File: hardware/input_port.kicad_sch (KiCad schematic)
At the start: 5 parts, among them J101 SS-74500-022

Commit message: Save
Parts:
- renumbered J101 to J301

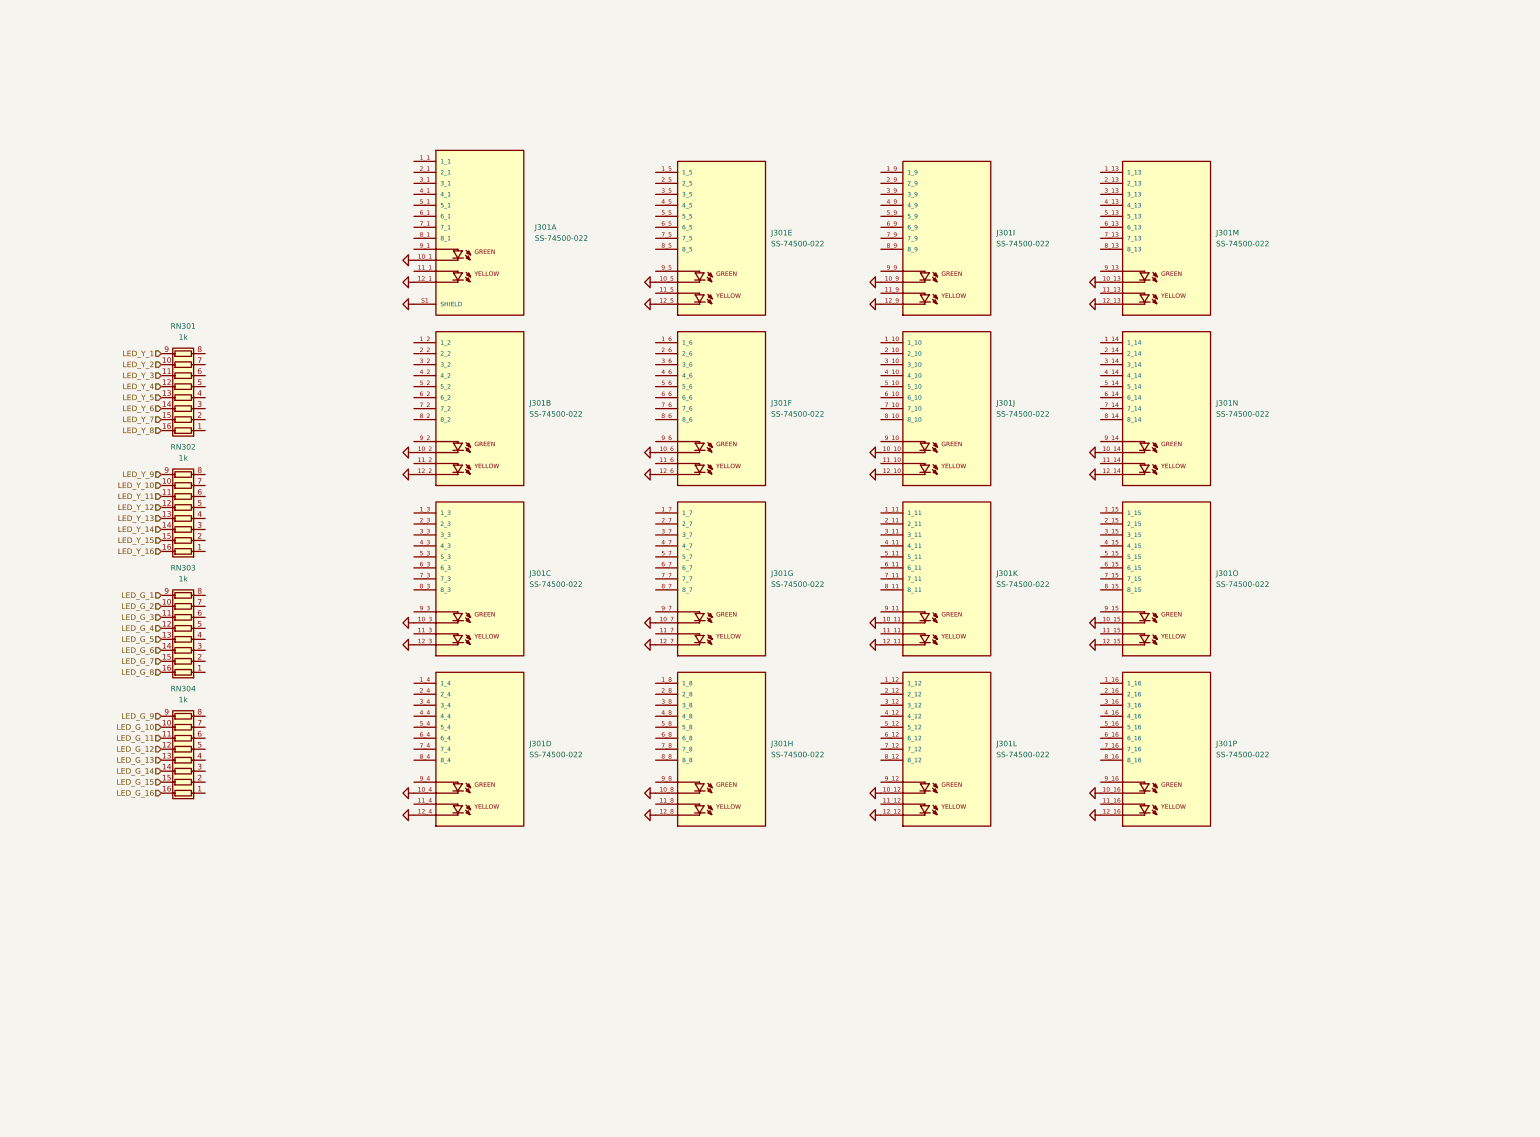
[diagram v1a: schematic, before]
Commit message: Moved to PCIe connectors, added USB 3.0 Type B connector
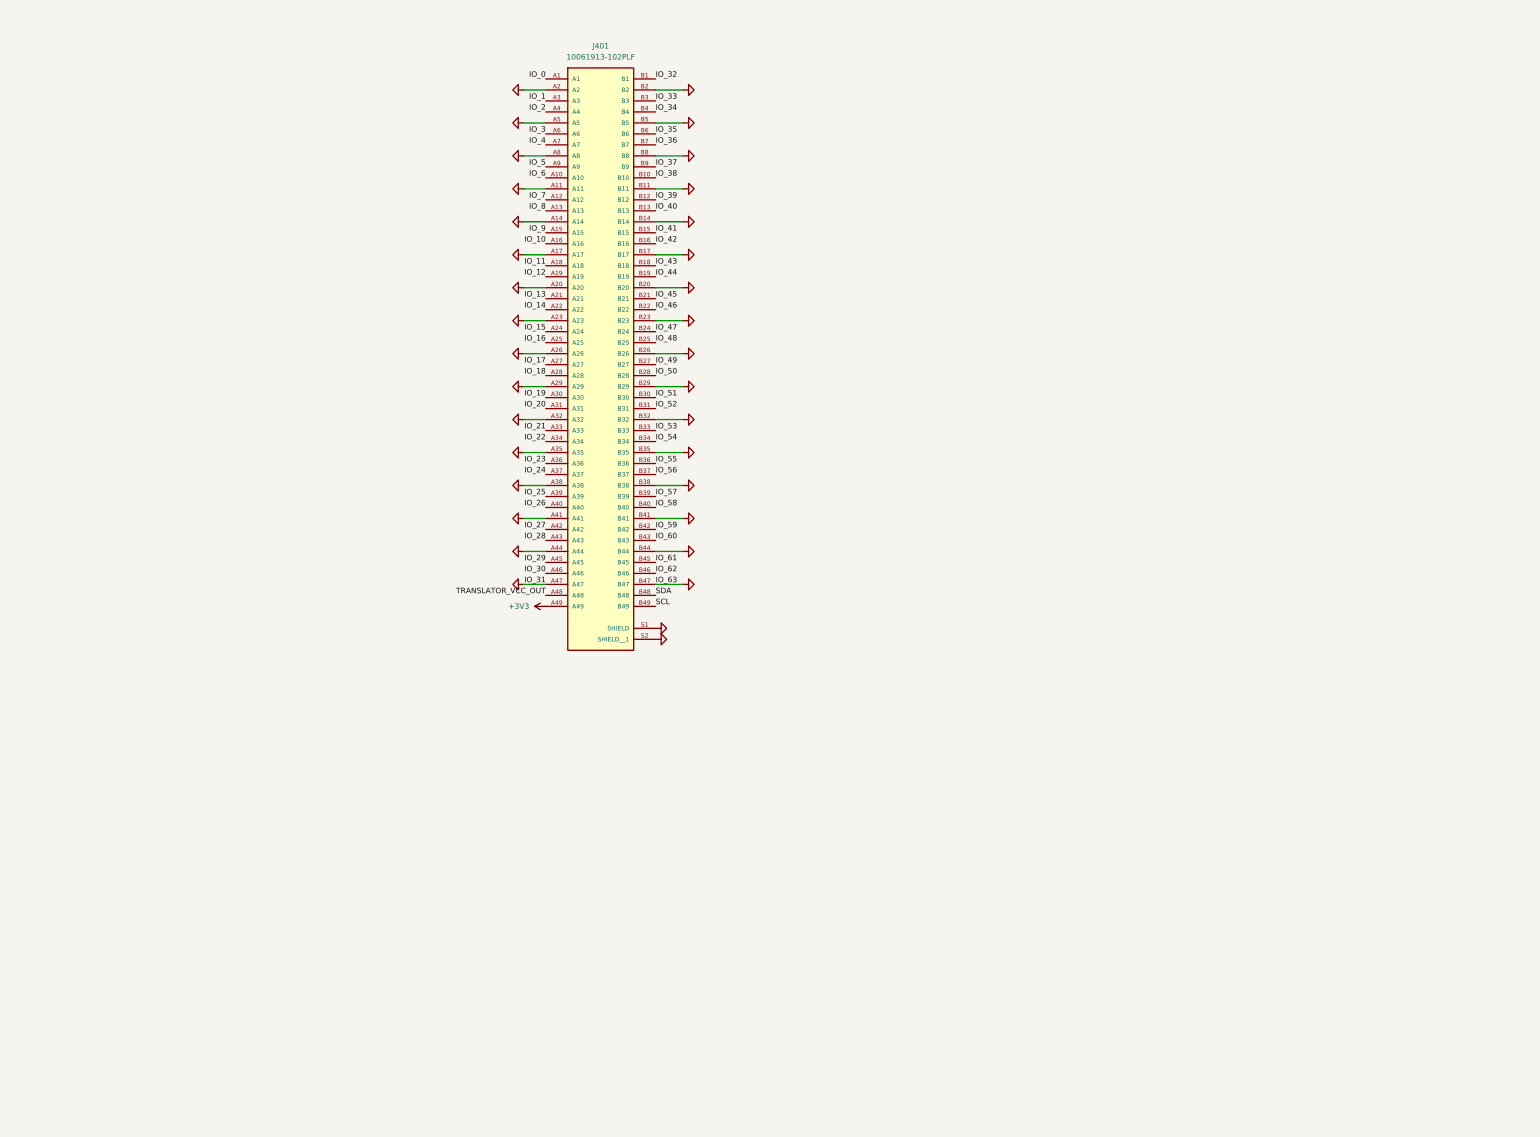
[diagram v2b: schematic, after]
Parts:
- removed J301: SS-74500-022, BEL_SS-74500-022, symbol connectors:SS-74500-022
- removed RN301, RN302, RN303, RN304: 1k, Resistor_SMD:R_Array_Convex_8x0602, symbol Device:R_Pack08
- added J401: 10061913-102PLF, connectors:AMPHENOL_10061913-102PLF, symbol connectors:10061913-102PLF
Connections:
- net GND: now also J401.A11, J401.A14, J401.A17, J401.A2, J401.A20, J401.A23, J401.A26, J401.A29, J401.A32, J401.A35, J401.A38, J401.A41, J401.A44, J401.A47, J401.A5, J401.A8, J401.B11, J401.B14, J401.B17, J401.B2, J401.B20, J401.B23, J401.B26, J401.B29, J401.B32, J401.B35, J401.B38, J401.B41, J401.B44, J401.B47, J401.B5, J401.B8, J401.S1 (SHIELD), J401.S2 (SHIELD__1)
- new net +3V3: J401.A49
- new net IO_0: J401.A1
- new net IO_1: J401.A3
- new net IO_10: J401.A16
- new net IO_11: J401.A18
- new net IO_12: J401.A19
- new net IO_13: J401.A21
- new net IO_14: J401.A22
- new net IO_15: J401.A24
- new net IO_16: J401.A25
- new net IO_17: J401.A27
- new net IO_18: J401.A28
- new net IO_19: J401.A30
- new net IO_2: J401.A4
- new net IO_20: J401.A31
- new net IO_21: J401.A33
- new net IO_22: J401.A34
- new net IO_23: J401.A36
- new net IO_24: J401.A37
- new net IO_25: J401.A39
- new net IO_26: J401.A40
- new net IO_27: J401.A42
- new net IO_28: J401.A43
- new net IO_29: J401.A45
- new net IO_3: J401.A6
- new net IO_30: J401.A46
- new net IO_32: J401.B1
- new net IO_33: J401.B3
- new net IO_34: J401.B4
- new net IO_35: J401.B6
- new net IO_36: J401.B7
- new net IO_37: J401.B9
- new net IO_38: J401.B10
- new net IO_39: J401.B12
- new net IO_4: J401.A7
- new net IO_40: J401.B13
- new net IO_41: J401.B15
- new net IO_42: J401.B16
- new net IO_43: J401.B18
- new net IO_44: J401.B19
- new net IO_45: J401.B21
- new net IO_46: J401.B22
- new net IO_47: J401.B24
- new net IO_48: J401.B25
- new net IO_49: J401.B27
- new net IO_5: J401.A9
- new net IO_50: J401.B28
- new net IO_51: J401.B30
- new net IO_52: J401.B31
- new net IO_53: J401.B33
- new net IO_54: J401.B34
- new net IO_55: J401.B36
- new net IO_56: J401.B37
- new net IO_57: J401.B39
- new net IO_58: J401.B40
- new net IO_59: J401.B42
- new net IO_6: J401.A10
- new net IO_60: J401.B43
- new net IO_61: J401.B45
- new net IO_62: J401.B46
- new net IO_7: J401.A12
- new net IO_8: J401.A13
- new net IO_9: J401.A15
- new net SCL: J401.B49
- new net SDA: J401.B48
- new net TRANSLATOR_VCC_OUT: J401.A48

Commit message: Save
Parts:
- added C301, C302, C303, C304, C305, C306, C307, C308, C309, C310, C311, C312, C313, C314, C315, C316: 0.1u, passive:C_0201, symbol Device:C_Small
- added U301, U303, U305, U307, U309, U310, U311, U312: TXB0108DQSR, Package_SON:USON-20_2x4mm_P0.4mm, symbol Logic_LevelTranslator:TXB0108DQSR
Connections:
- net TRANSLATOR_VCC_OUT is gone; now on net GND: J401.A48
- net +3V3: now also J401.B48, C301.1, C302.1, C303.1, C304.1, C305.1, C306.1, C307.1, C308.1, U301.5 (VCCA), U303.5 (VCCA), U305.5 (VCCA), U307.5 (VCCA), U309.5 (VCCA), U310.5 (VCCA), U311.5 (VCCA), U312.5 (VCCA); no longer J401.A49
- net GND: now also C301.2, C302.2, C303.2, C304.2, C305.2, C306.2, C307.2, C308.2, C309.2, C310.2, C311.2, C312.2, C313.2, C314.2, C315.2, C316.2, U301.15 (GND), U303.15 (GND), U305.15 (GND), U307.15 (GND), U309.15 (GND), U310.15 (GND), U311.15 (GND), U312.15 (GND); no longer J401.A47, J401.B47
- net IO_0: now also U301.10 (A8); no longer J401.A1
- net IO_1: now also U301.9 (A7); no longer J401.A3
- net IO_10: now also U303.8 (A6); no longer J401.A16
- net IO_11: now also U303.7 (A5); no longer J401.A18
- net IO_12: now also U303.4 (A4); no longer J401.A19
- net IO_13: now also U303.3 (A3); no longer J401.A21
- net IO_14: now also U303.2 (A2); no longer J401.A22
- net IO_15: now also U303.1 (A1); no longer J401.A24
- net IO_16: now also U305.10 (A8); no longer J401.A25
- net IO_17: now also U305.9 (A7); no longer J401.A27
- net IO_18: now also U305.8 (A6); no longer J401.A28
- net IO_19: now also U305.7 (A5); no longer J401.A30
- net IO_2: now also U301.8 (A6); no longer J401.A4
- net IO_20: now also U305.4 (A4); no longer J401.A31
- net IO_21: now also U305.3 (A3); no longer J401.A33
- net IO_22: now also U305.2 (A2); no longer J401.A34
- net IO_23: now also U305.1 (A1); no longer J401.A36
- net IO_24: now also U307.10 (A8); no longer J401.A37
- net IO_25: now also U307.9 (A7); no longer J401.A39
- net IO_26: now also U307.8 (A6); no longer J401.A40
- net IO_27: now also U307.7 (A5); no longer J401.A42
- net IO_28: now also U307.4 (A4); no longer J401.A43
- net IO_29: now also U307.3 (A3); no longer J401.A45
- net IO_3: now also U301.7 (A5); no longer J401.A6
- net IO_30: now also U307.2 (A2); no longer J401.A46
- net IO_32: now also U309.1 (A1); no longer J401.B1
- net IO_33: now also U309.2 (A2); no longer J401.B3
- net IO_34: now also U309.3 (A3); no longer J401.B4
- net IO_35: now also U309.4 (A4); no longer J401.B6
- net IO_36: now also U309.7 (A5); no longer J401.B7
- net IO_37: now also U309.8 (A6); no longer J401.B9
- net IO_38: now also U309.9 (A7); no longer J401.B10
- net IO_39: now also U309.10 (A8); no longer J401.B12
- net IO_4: now also U301.4 (A4); no longer J401.A7
- net IO_40: now also U310.1 (A1); no longer J401.B13
- net IO_41: now also U310.2 (A2); no longer J401.B15
- net IO_42: now also U310.3 (A3); no longer J401.B16
- net IO_43: now also U310.4 (A4); no longer J401.B18
- net IO_44: now also U310.7 (A5); no longer J401.B19
- net IO_45: now also U310.8 (A6); no longer J401.B21
- net IO_46: now also U310.9 (A7); no longer J401.B22
- net IO_47: now also U310.10 (A8); no longer J401.B24
- net IO_48: now also U311.1 (A1); no longer J401.B25
- net IO_49: now also U311.2 (A2); no longer J401.B27
- net IO_5: now also U301.3 (A3); no longer J401.A9
- net IO_50: now also U311.3 (A3); no longer J401.B28
- net IO_51: now also U311.4 (A4); no longer J401.B30
- net IO_52: now also U311.7 (A5); no longer J401.B31
- net IO_53: now also U311.8 (A6); no longer J401.B33
- net IO_54: now also U311.9 (A7); no longer J401.B34
- net IO_55: now also U311.10 (A8); no longer J401.B36
- net IO_56: now also U312.1 (A1); no longer J401.B37
- net IO_57: now also U312.2 (A2); no longer J401.B39
- net IO_58: now also U312.3 (A3); no longer J401.B40
- net IO_59: now also U312.4 (A4); no longer J401.B42
- net IO_6: now also U301.2 (A2); no longer J401.A10
- net IO_60: now also U312.7 (A5); no longer J401.B43
- net IO_61: now also U312.8 (A6); no longer J401.B45
- net IO_62: now also U312.9 (A7); no longer J401.B46
- net IO_7: now also U301.1 (A1); no longer J401.A12
- net IO_8: now also U303.10 (A8); no longer J401.A13
- net IO_9: now also U303.9 (A7); no longer J401.A15
- net SDA: now also J401.A49; no longer J401.B48
- new net IO_31: U307.1 (A1)
- new net IO_63: U312.10 (A8)
- new net IO_C_0: J401.A1, U301.11 (B8)
- new net IO_C_1: J401.A3, U301.12 (B7)
- new net IO_C_10: J401.A16, U303.13 (B6)
- new net IO_C_11: J401.A18, U303.14 (B5)
- new net IO_C_12: J401.A19, U303.17 (B4)
- new net IO_C_13: J401.A21, U303.18 (B3)
- new net IO_C_14: J401.A22, U303.19 (B2)
- new net IO_C_15: J401.A24, U303.20 (B1)
- new net IO_C_16: J401.A25, U305.11 (B8)
- new net IO_C_17: J401.A27, U305.12 (B7)
- new net IO_C_18: J401.A28, U305.13 (B6)
- new net IO_C_19: J401.A30, U305.14 (B5)
- new net IO_C_2: J401.A4, U301.13 (B6)
- new net IO_C_20: J401.A31, U305.17 (B4)
- new net IO_C_21: J401.A33, U305.18 (B3)
- new net IO_C_22: J401.A34, U305.19 (B2)
- new net IO_C_23: J401.A36, U305.20 (B1)
- new net IO_C_24: J401.A37, U307.11 (B8)
- new net IO_C_25: J401.A39, U307.12 (B7)
- new net IO_C_26: J401.A40, U307.13 (B6)
- new net IO_C_27: J401.A42, U307.14 (B5)
- new net IO_C_28: J401.A43, U307.17 (B4)
- new net IO_C_29: J401.A45, U307.18 (B3)
- new net IO_C_3: J401.A6, U301.14 (B5)
- new net IO_C_30: J401.A46, U307.19 (B2)
- new net IO_C_31: J401.A47, U307.20 (B1)
- new net IO_C_32: J401.B1, U309.20 (B1)
- new net IO_C_33: J401.B3, U309.19 (B2)
- new net IO_C_34: J401.B4, U309.18 (B3)
- new net IO_C_35: J401.B6, U309.17 (B4)
- new net IO_C_36: J401.B7, U309.14 (B5)
- new net IO_C_37: J401.B9, U309.13 (B6)
- new net IO_C_38: J401.B10, U309.12 (B7)
- new net IO_C_39: J401.B12, U309.11 (B8)
- new net IO_C_4: J401.A7, U301.17 (B4)
- new net IO_C_40: J401.B13, U310.20 (B1)
- new net IO_C_41: J401.B15, U310.19 (B2)
- new net IO_C_42: J401.B16, U310.18 (B3)
- new net IO_C_43: J401.B18, U310.17 (B4)
- new net IO_C_44: J401.B19, U310.14 (B5)
- new net IO_C_45: J401.B21, U310.13 (B6)
- new net IO_C_46: J401.B22, U310.12 (B7)
- new net IO_C_47: J401.B24, U310.11 (B8)
- new net IO_C_48: J401.B25, U311.20 (B1)
- new net IO_C_49: J401.B27, U311.19 (B2)
- new net IO_C_5: J401.A9, U301.18 (B3)
- new net IO_C_50: J401.B28, U311.18 (B3)
- new net IO_C_51: J401.B30, U311.17 (B4)
- new net IO_C_52: J401.B31, U311.14 (B5)
- new net IO_C_53: J401.B33, U311.13 (B6)
- new net IO_C_54: J401.B34, U311.12 (B7)
- new net IO_C_55: J401.B36, U311.11 (B8)
- new net IO_C_56: J401.B37, U312.20 (B1)
- new net IO_C_57: J401.B39, U312.19 (B2)
- new net IO_C_58: J401.B40, U312.18 (B3)
- new net IO_C_59: J401.B42, U312.17 (B4)
- new net IO_C_6: J401.A10, U301.19 (B2)
- new net IO_C_60: J401.B43, U312.14 (B5)
- new net IO_C_61: J401.B45, U312.13 (B6)
- new net IO_C_62: J401.B46, U312.12 (B7)
- new net IO_C_63: J401.B47, U312.11 (B8)
- new net IO_C_7: J401.A12, U301.20 (B1)
- new net IO_C_8: J401.A13, U303.11 (B8)
- new net IO_C_9: J401.A15, U303.12 (B7)
- new net PORT_ENABLE: U301.6 (OE), U303.6 (OE), U305.6 (OE), U307.6 (OE), U309.6 (OE), U310.6 (OE), U311.6 (OE), U312.6 (OE)
- new net Vdrive: C309.1, C310.1, C311.1, C312.1, C313.1, C314.1, C315.1, C316.1, U301.16 (VCCB), U303.16 (VCCB), U305.16 (VCCB), U307.16 (VCCB), U309.16 (VCCB), U310.16 (VCCB), U311.16 (VCCB), U312.16 (VCCB)
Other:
- moved on the sheet: J401

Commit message: Save
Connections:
- net +3V3: no longer C301.1, C302.1, C303.1, C304.1, C305.1, C306.1, C307.1, C308.1, U301.5 (VCCA), U303.5 (VCCA), U305.5 (VCCA), U307.5 (VCCA), U309.5 (VCCA), U310.5 (VCCA), U311.5 (VCCA), U312.5 (VCCA)
- new net +1V5: C301.1, C302.1, C303.1, C304.1, C305.1, C306.1, C307.1, C308.1, U301.5 (VCCA), U303.5 (VCCA), U305.5 (VCCA), U307.5 (VCCA), U309.5 (VCCA), U310.5 (VCCA), U311.5 (VCCA), U312.5 (VCCA)
